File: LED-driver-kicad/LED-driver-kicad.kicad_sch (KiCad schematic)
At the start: 28 parts, among them SW1 SW_SPST, U2 NCP1095DBR2, U4 25AA02E64-I/SN, U5 PIC18F97J60-IPF, Y1 25MHz

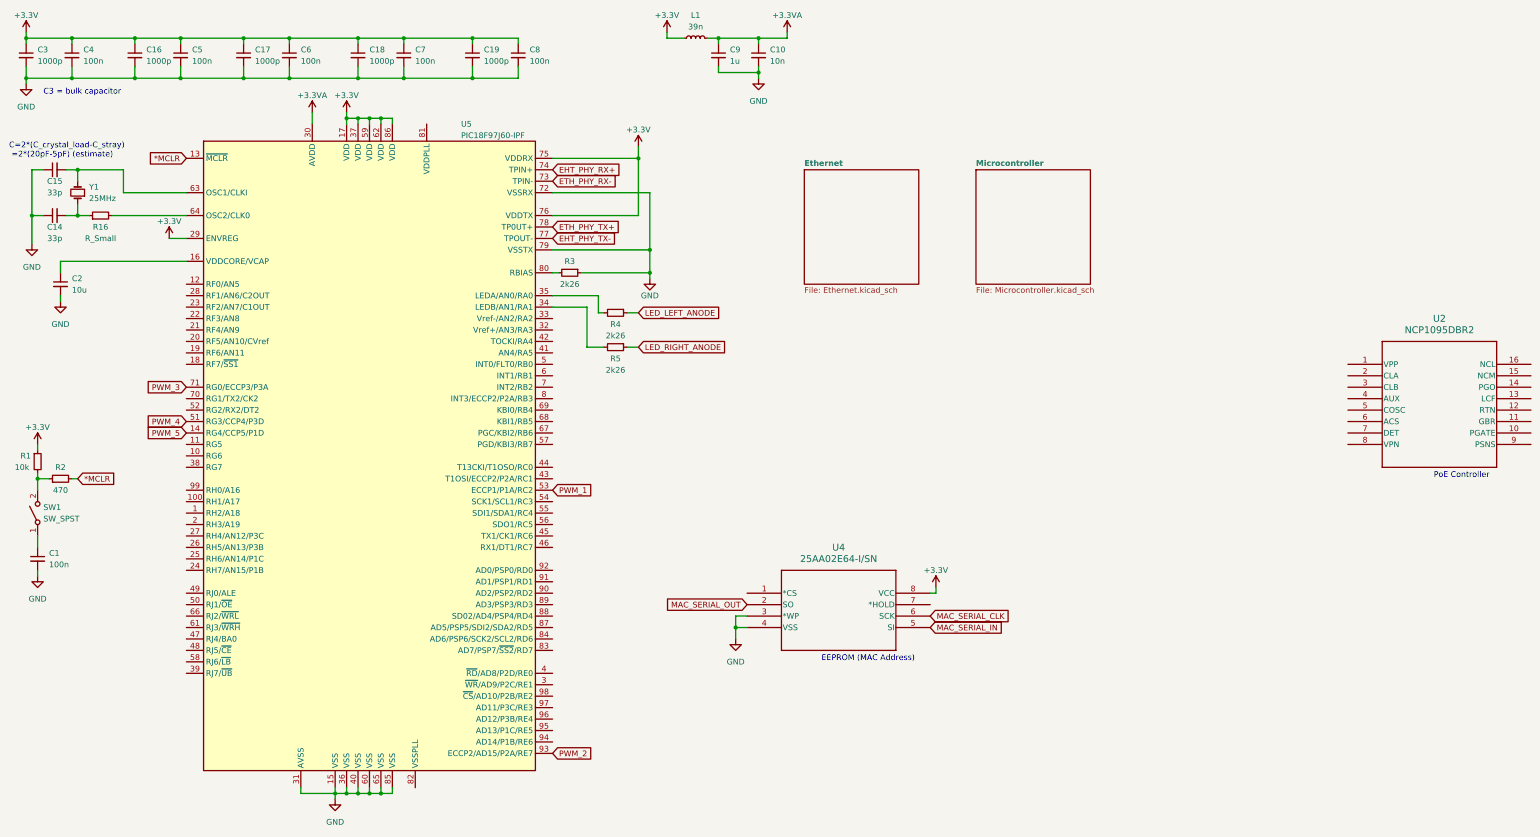
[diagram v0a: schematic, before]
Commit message: update main schematic sheet and microcontroller
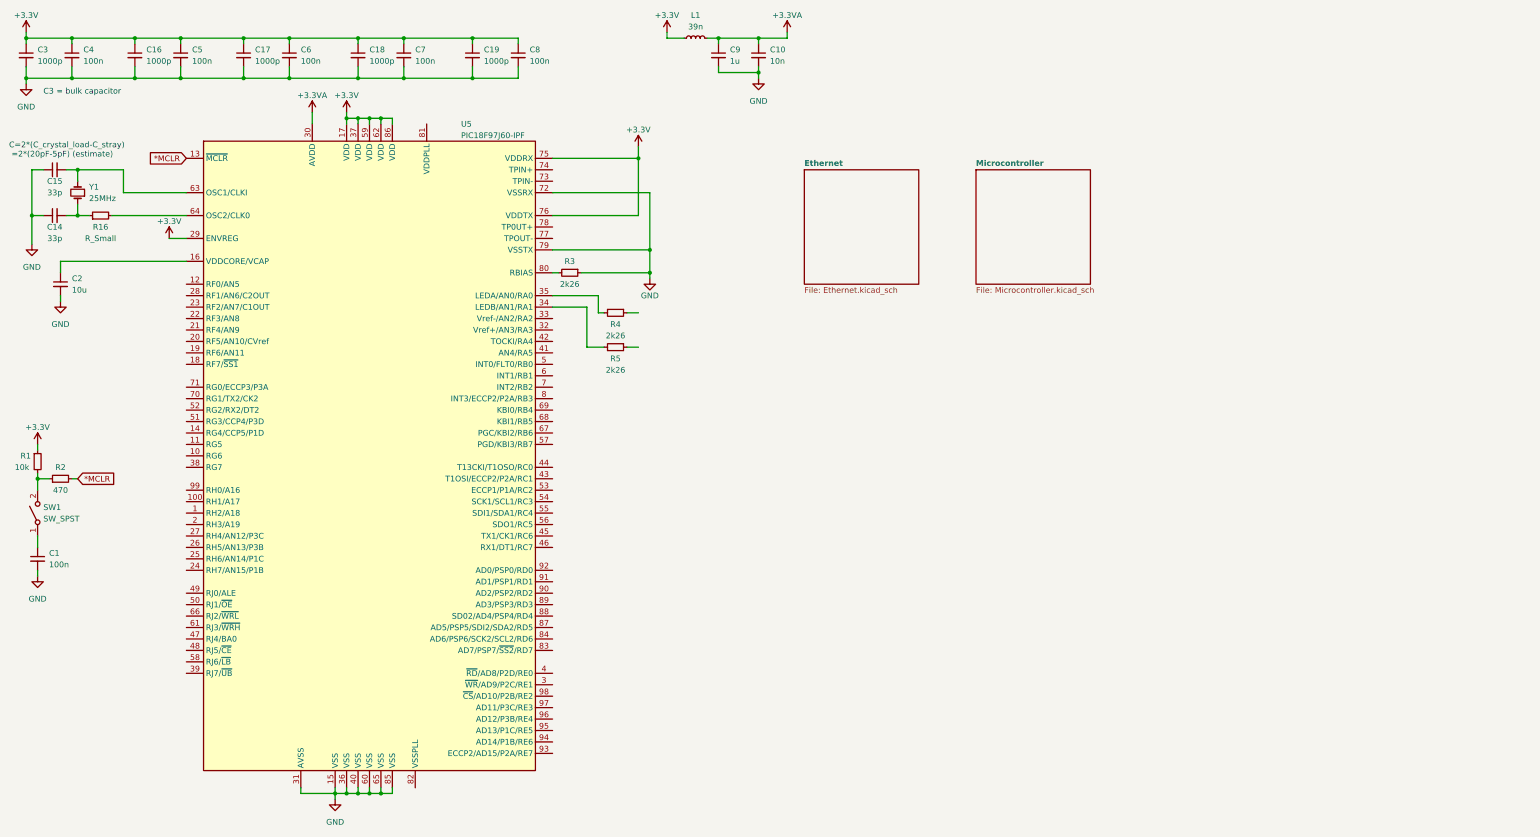
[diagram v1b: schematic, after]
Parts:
- removed U2: NCP1095DBR2, TSSOP-16_948F-01_OSI, symbol NCP1095DBR2:NCP1095DBR2
- removed U4: 25AA02E64-I/SN, SOIC8_4P9X3P9MC_MCH, symbol 25AA02E64-I/SN:25AA02E64-I_SN
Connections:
- net EHT_PHY_RX+: no longer names the net of U5.74 (TPIN+)
- net EHT_PHY_TX-: no longer names the net of U5.77 (TPOUT-)
- net ETH_PHY_RX-: no longer names the net of U5.73 (TPIN-)
- net ETH_PHY_TX+: no longer names the net of U5.78 (TP0UT+)
- net LED_LEFT_ANODE: no longer names the net of R4.1
- net LED_RIGHT_ANODE: no longer names the net of R5.1
- net PWM_1: no longer names the net of U5.53 (ECCP1/P1A/RC2)
- net PWM_2: no longer names the net of U5.93 (ECCP2/AD15/P2A/RE7)
- net PWM_3: no longer names the net of U5.71 (RG0/ECCP3/P3A)
- net PWM_4: no longer names the net of U5.51 (RG3/CCP4/P3D)
- net PWM_5: no longer names the net of U5.14 (RG4/CCP5/P1D)
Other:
- note removed: "EEPROM (MAC Address)"
- note removed: "PoE Controller"

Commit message: remove unused libraries
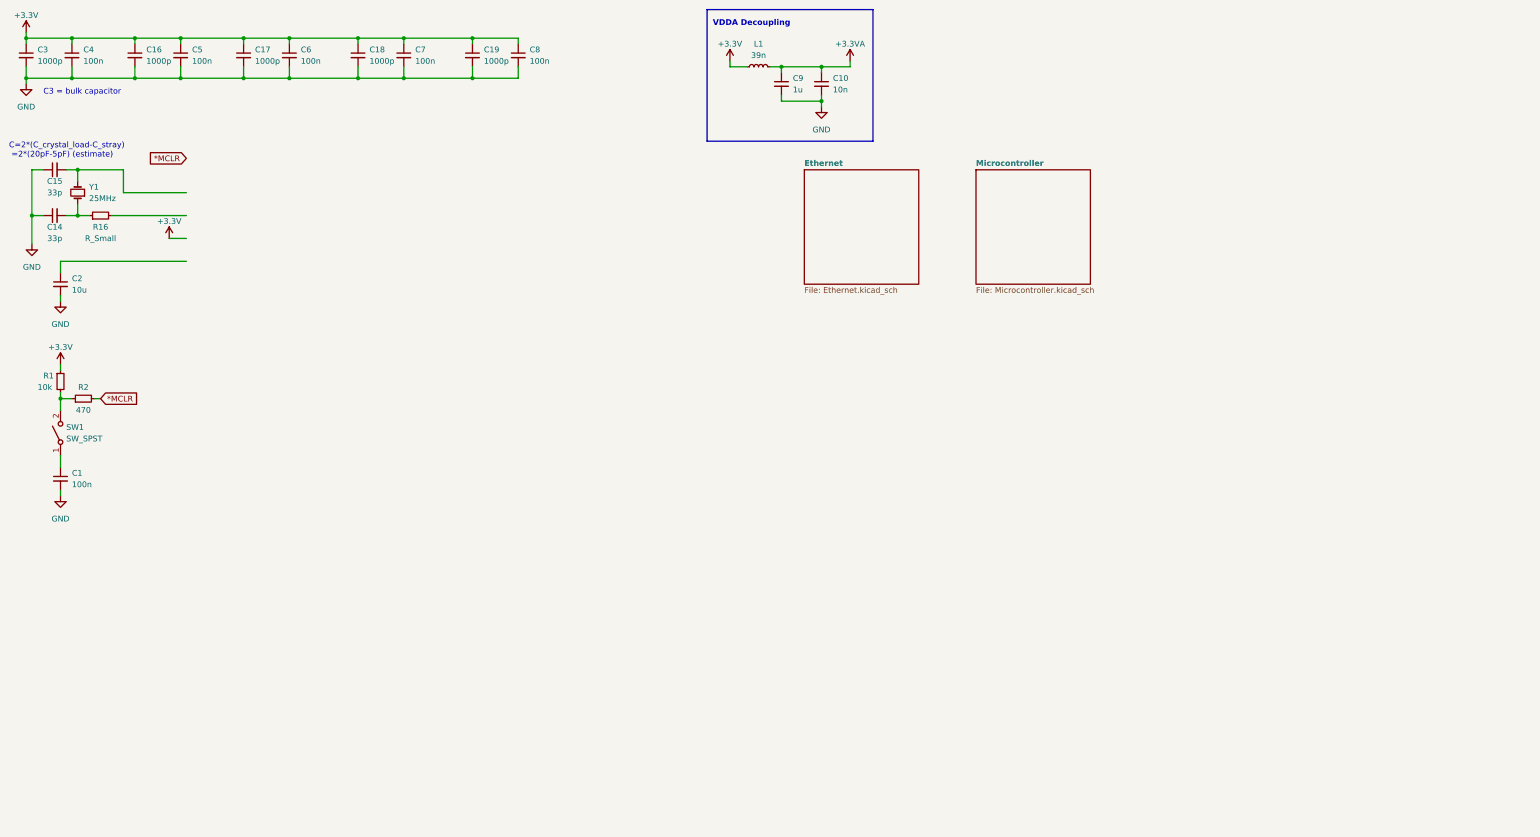
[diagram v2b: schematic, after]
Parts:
- removed R3, R4, R5: 2k26, symbol Device:R_Small
- removed U5: PIC18F97J60-IPF, Package_QFP:TQFP-100_12x12mm_P0.4mm, symbol MCU_Microchip_PIC18:PIC18F97J60-IPF
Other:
- note added: "VDDA Decoupling"
- moved on the sheet: C1, C10, C9, L1, R1, R2, SW1

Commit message: update main schematic sheet
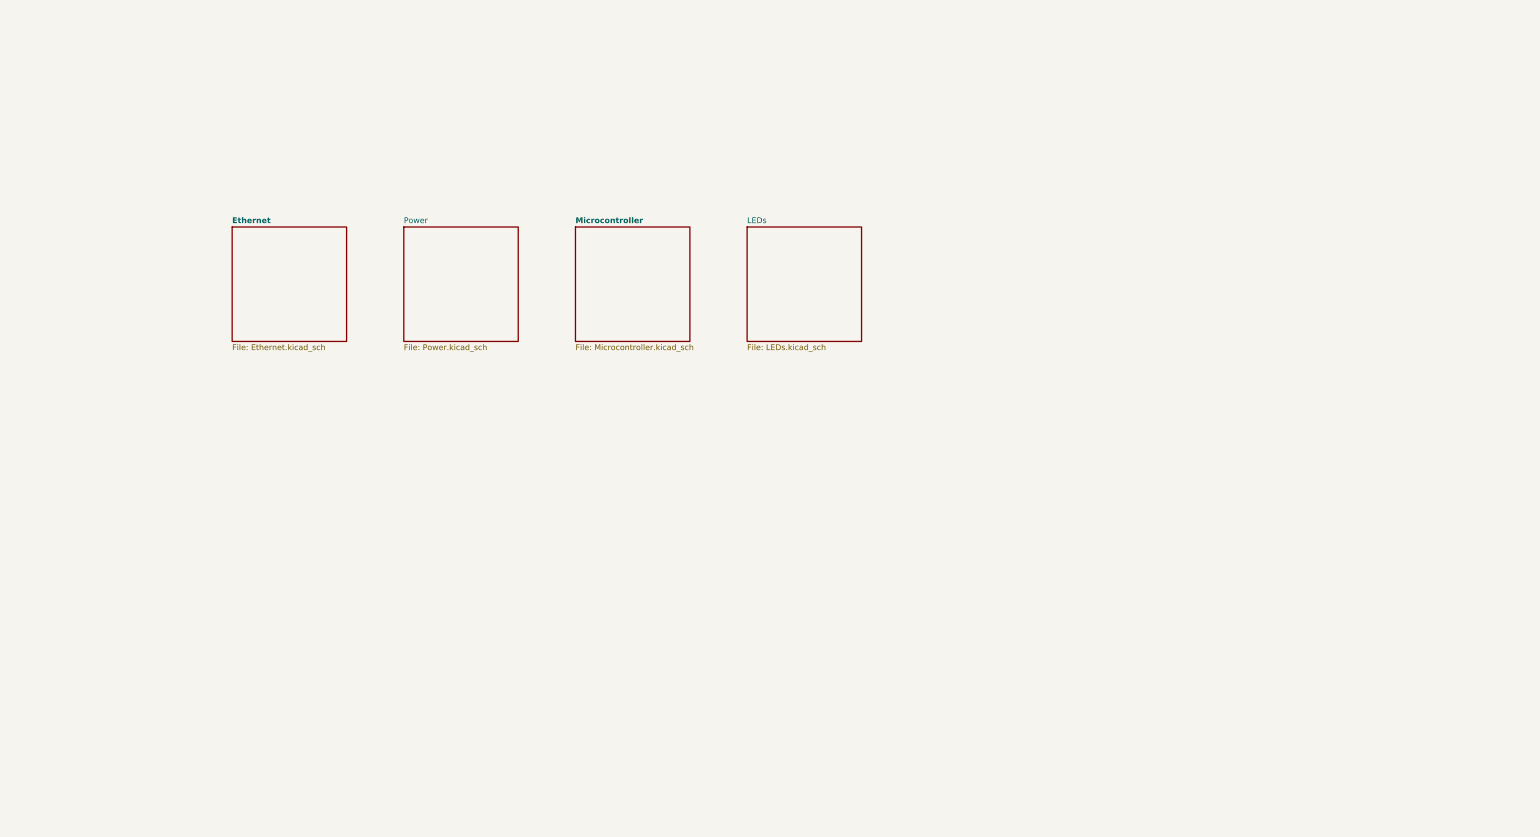
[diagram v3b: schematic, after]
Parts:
- removed C1: 100n, symbol Device:C_Small
- removed C10: 10n, symbol Device:C_Small
- removed C14, C15: 33p, symbol Device:C_Small
- removed C16, C17, C18, C3: 1000p, symbol Device:C_Small
- removed C19: 1000p, Capacitor_SMD:C_1206_3216Metric_Pad1.33x1.80mm_HandSolder, symbol Device:C_Small
- removed C2: 10u, symbol Device:C_Small
- removed C4, C5, C6, C7, C8: 100n, Capacitor_SMD:C_1206_3216Metric_Pad1.33x1.80mm_HandSolder, symbol Device:C_Small
- removed C9: 1u, symbol Device:C_Small
- removed L1: 39n, symbol Device:L_Small
- removed R1: 10k, symbol Device:R_Small
- removed R16: R_Small, symbol Device:R_Small
- removed R2: 470, symbol Device:R_Small
- removed SW1: SW_SPST, symbol Switch:SW_SPST
- removed Y1: 25MHz, symbol Device:Crystal_Small
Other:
- added sheet LEDs (LEDs.kicad_sch)
- added sheet Power (Power.kicad_sch)
- note removed: "C3 = bulk capacitor"
- note removed: "C=2*(C_crystal_load-C_stray) =2*(20pF-5pF) (estimate)"
- note removed: "VDDA Decoupling"

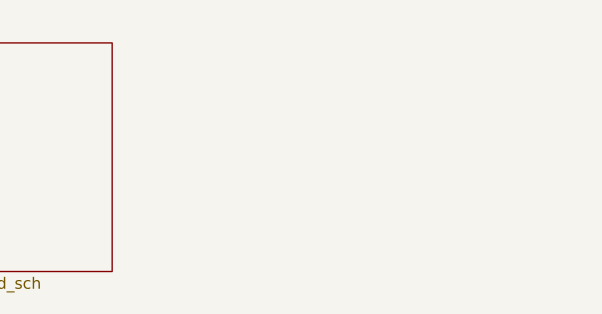
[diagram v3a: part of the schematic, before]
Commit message: add schematic sheet for white and PC amber LED
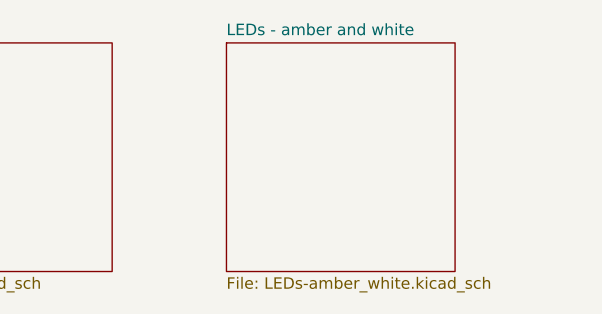
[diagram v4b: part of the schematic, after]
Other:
- added sheet LEDs - amber and white (LEDs-amber_white.kicad_sch)
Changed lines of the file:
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@@
+    )
+  )
+  (sheet (at 215.9 63.5) (size 25.4 25.4) (fields_autoplaced)
+    (stroke (width 0.1524) (type solid))
+    (fill (color 0 255 0 1.0000))
+    (property "Sheetname" "LEDs - amber and white" (at 215.9 62.7884 0)
+      (effects (font (size 1.27 1.27)) (justify left bottom))
+    )
+    (property "Sheetfile" "LEDs-amber_white.kicad_sch" (at 215.9 89.4846 0)
+      (effects (font (size 1.27 1.27)) (justify left top))
+    )
+    (instances
+      (project "LED-driver-kicad"
+        (path "/2b071084-2ab6-4896-84cc-45b211479417" (page "6"))
+      )
     )
   )

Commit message: update comments and title blocks
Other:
- title: (none) -> Photogrammetry Rig - LED Driver
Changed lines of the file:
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@@
 (kicad_sch (version 20230121) (generator eeschema)
   (paper "A4")
+  (title_block
+    (title "Photogrammetry Rig - LED Driver")
+    (date "2023-08-02")
+    (rev "0.1.0")
+  )
   (sheet (at 101.6 63.5) (size 25.4 25.4) (fields_autoplaced)
     (stroke (width 0.1524) (type solid))

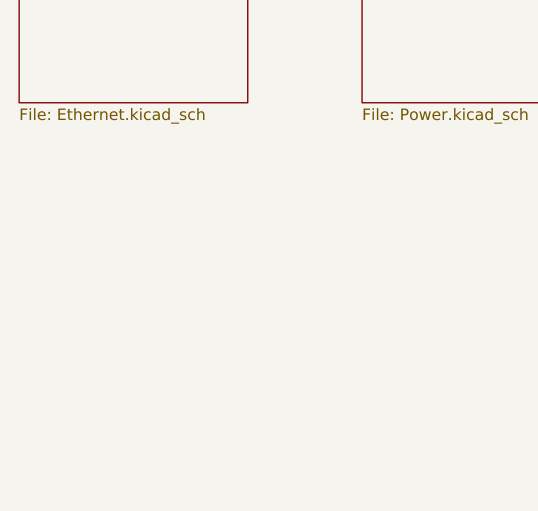
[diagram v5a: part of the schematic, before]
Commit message: update initial components layout
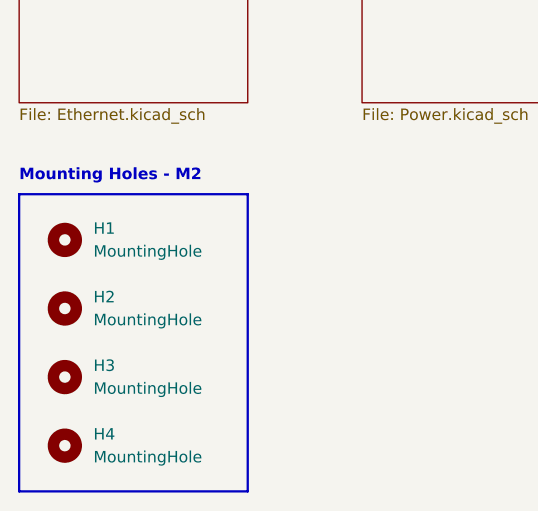
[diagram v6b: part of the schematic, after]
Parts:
- added H1, H2, H3, H4: MountingHole, MountingHole:MountingHole_3.2mm_M3, symbol Mechanical:MountingHole
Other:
- note added: "Mounting Holes - M2"
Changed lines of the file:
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@@
     (rev "0.1.0")
+  )
+  (rectangle (start 63.5 99.06) (end 88.9 132.08)
+    (stroke (width 0.254) (type solid))
+    (fill (type none))
+  )
+  (text "Mounting Holes - M2" (at 63.5 97.79 0)
+    (effects (font (size 1.27 1.27) (thickness 0.254) bold) (justify left bottom))
+  )
+  (symbol (lib_id "Mechanical:MountingHole") (at 68.58 111.76 0) (unit 1)
+    (in_bom yes) (on_board yes) (dnp no) (fields_autoplaced)
+    (property "Reference" "H2" (at 71.755 110.49 0)
+      (effects (font (size 1.27 1.27)) (justify left))
+    )
+    (property "Value" "MountingHole" (at 71.755 113.03 0)
+      (effects (font (size 1.27 1.27)) (justify left))
+    )
+    (property "Footprint" "MountingHole:MountingHole_3.2mm_M3" (at 68.58 111.76 0)
+      (effects (font (size 1.27 1.27)) hide)
+    )
+    (property "Datasheet" "~" (at 68.58 111.76 0)
+      (effects (font (size 1.27 1.27)) hide)
+    )
+    (instances
+      (project "LED-driver-kicad"
+        (path "/2b071084-2ab6-4896-84cc-45b211479417"
+          (reference "H2") (unit 1)
+        )
+      )
+    )
+  )
+  (symbol (lib_id "Mechanical:MountingHole") (at 68.58 104.14 0) (unit 1)
+    (in_bom yes) (on_board yes) (dnp no) (fields_autoplaced)
+    (property "Reference" "H1" (at 71.755 102.87 0)
+      (effects (font (size 1.27 1.27)) (justify left))
+    )
+    (property "Value" "MountingHole" (at 71.755 105.41 0)
+      (effects (font (size 1.27 1.27)) (justify left))
+    )
+    (property "Footprint" "MountingHole:MountingHole_3.2mm_M3" (at 68.58 104.14 0)
+      (effects (font (size 1.27 1.27)) hide)
+    )
+    (property "Datasheet" "~" (at 68.58 104.14 0)
+      (effects (font (size 1.27 1.27)) hide)
+    )
+    (instances
+      (project "LED-driver-kicad"
+        (path "/2b071084-2ab6-4896-84cc-45b211479417"
+          (reference "H1") (unit 1)
+        )
+      )
+    )
+  )
+  (symbol (lib_id "Mechanical:MountingHole") (at 68.58 127 0) (unit 1)
+    (in_bom yes) (on_board yes) (dnp no) (fields_autoplaced)
+    (property "Reference" "H4" (at 71.755 125.73 0)
+      (effects (font (size 1.27 1.27)) (justify left))
+    )
+    (property "Value" "MountingHole" (at 71.755 128.27 0)
+      (effects (font (size 1.27 1.27)) (justify left))
+    )
+    (property "Footprint" "MountingHole:MountingHole_3.2mm_M3" (at 68.58 127 0)
+      (effects (font (size 1.27 1.27)) hide)
+    )
+    (property "Datasheet" "~" (at 68.58 127 0)
+      (effects (font (size 1.27 1.27)) hide)
+    )
+    (instances
+      (project "LED-driver-kicad"
+        (path "/2b071084-2ab6-4896-84cc-45b211479417"
+          (reference "H4") (unit 1)
+        )
+      )
+    )
+  )
+  (symbol (lib_id "Mechanical:MountingHole") (at 68.58 119.38 0) (unit 1)
+    (in_bom yes) (on_board yes) (dnp no) (fields_autoplaced)
+    (property "Reference" "H3" (at 71.755 118.11 0)
+      (effects (font (size 1.27 1.27)) (justify left))
+    )
+    (property "Value" "MountingHole" (at 71.755 120.65 0)
+      (effects (font (size 1.27 1.27)) (justify left))
+    )
+    (property "Footprint" "MountingHole:MountingHole_3.2mm_M3" (at 68.58 119.38 0)
+      (effects (font (size 1.27 1.27)) hide)
+    )
+    (property "Datasheet" "~" (at 68.58 119.38 0)
+      (effects (font (size 1.27 1.27)) hide)
+    )
+    (instances
+      (project "LED-driver-kicad"
+        (path "/2b071084-2ab6-4896-84cc-45b211479417"
+          (reference "H3") (unit 1)
+        )
+      )
+    )
   )
   (sheet (at 101.6 63.5) (size 25.4 25.4) (fields_autoplaced)
